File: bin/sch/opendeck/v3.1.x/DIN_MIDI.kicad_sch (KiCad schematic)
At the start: 9 parts, among them J1 DIN-5, J2 DIN-5, U10 TLP2362

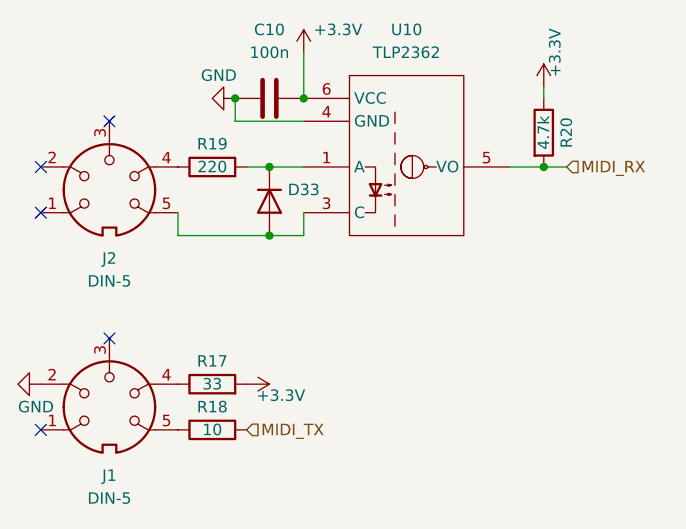
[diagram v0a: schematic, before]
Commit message: sch: update opendeck 3.1 schematics
replace SOIC-24 package for the multiplexers with TSSOP-24
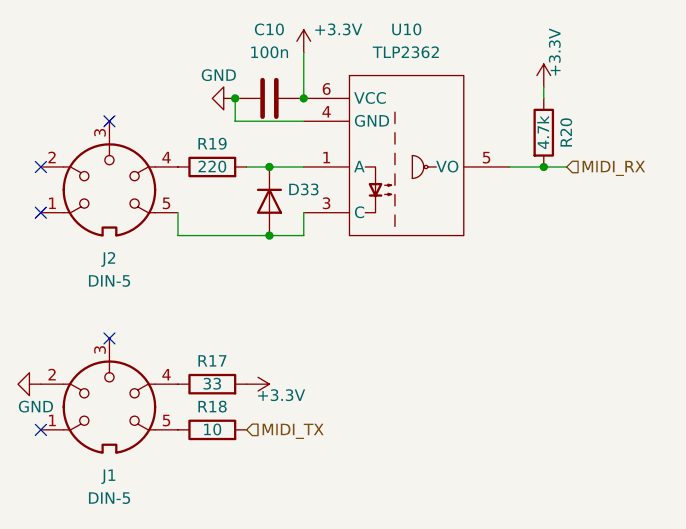
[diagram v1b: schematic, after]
